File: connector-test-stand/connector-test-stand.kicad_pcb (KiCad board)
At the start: 2 copper layers, 99.1 x 99.1 mm, 85 parts, among them J1 Conn_01x02, J10 Conn_01x04_MountingPin, J11 Conn_01x03_MountingPin, J12 DVI-I_Dual_Link, J2 Conn_01x02, J3 Conn_01x02, J4 Conn_01x05, J5 Conn_01x04_MountingPin, J6 Conn_01x02, J7 Conn_01x03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

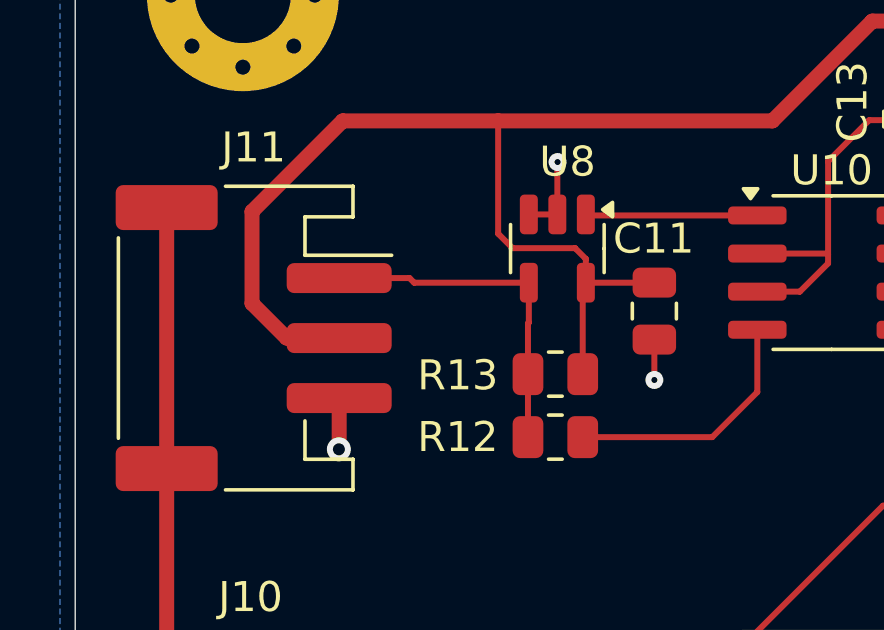
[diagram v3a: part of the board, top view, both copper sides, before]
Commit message: Add values for SMAART wire conevrter and safety rezistor
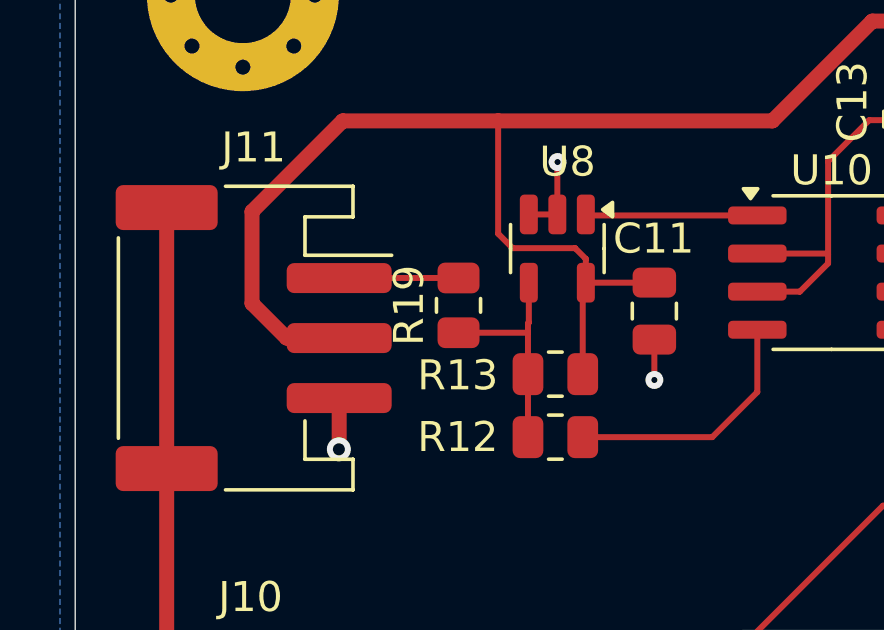
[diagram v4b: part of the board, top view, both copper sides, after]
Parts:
- added R19: 10R, Resistor_SMD:R_0805_2012Metric, F.Cu at (295.7, 121.1)
- R12: value R -> 100R
- R13: value R -> 4K1
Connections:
- R12 pad 2: Net-(J11-Pin_1) -> Net-(R12-Pad2)
- R13 pad 2: Net-(J11-Pin_1) -> Net-(R12-Pad2)
- U8 pad 4: Net-(J11-Pin_1) -> Net-(R12-Pad2)
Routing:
- net Net-(J11-Pin_1): track 11.5 -> 3.98 mm
- net Net-(R12-Pad2): track 0.00 -> 7.47 mm
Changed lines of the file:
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@@
 	(net 96 "TX")
 	(net 97 "Net-(U10-DE)")
+	(net 98 "Net-(R12-Pad2)")
 	(footprint "Potentiometer_THT:Potentiometer_Bourns_3266W_Vertical"
 		(layer "F.Cu")
@@
 			(layers "F.Cu" "F.Mask" "F.Paste")
 			(roundrect_rratio 0.25)
-			(net 51 "Net-(J11-Pin_1)")
+			(net 98 "Net-(R12-Pad2)")
 			(pintype "tri_state")
 		)
@@
 			)
 		)
-		(property "Value" "R"
+		(property "Value" "100R"
 			(at 0 1.65 0)
 			(layer "F.Fab")
@@
 			(layers "F.Cu" "F.Mask" "F.Paste")
 			(roundrect_rratio 0.243902)
-			(net 51 "Net-(J11-Pin_1)")
+			(net 98 "Net-(R12-Pad2)")
 			(pintype "passive")
 		)
@@
 			)
 		)
-		(property "Value" "R"
+		(property "Value" "4K1"
 			(at 0 1.65 0)
 			(layer "F.Fab")
@@
 			(layers "F.Cu" "F.Mask" "F.Paste")
 			(roundrect_rratio 0.243902)
-			(net 51 "Net-(J11-Pin_1)")
+			(net 98 "Net-(R12-Pad2)")
 			(pintype "passive")
 		)
@@
 		)
 	)
+	(footprint "Resistor_SMD:R_0805_2012Metric"
+		(layer "F.Cu")
+		(at 295.7322 121.0837 90)
+		(descr "Resistor SMD 0805 (2012 Metric), square (rectangular) end terminal, IPC-7351 nominal, (Body size source: IPC-SM-782 page 72, https://www.pcb-3d.com/wordpress/wp-content/uploads/ipc-sm-782a_amendment_1_and_2.pdf), generated with kicad-footprint-generator")
+		(tags "resistor")
+		(property "Reference" "R19"
+			(at 0 -1.65 90)
+			(layer "F.SilkS")
+			(effects
+				(font
+					(size 1 1)
+					(thickness 0.15)
+				)
+			)
+		)
+		(property "Value" "10R"
+			(at 0 1.65 90)
+			(layer "F.Fab")
+			(effects
+				(font
+					(size 1 1)
+					(thickness 0.15)
+				)
+			)
+		)
+		(property "Datasheet" ""
+			(at 0 0 90)
+			(layer "F.Fab")
+			(hide yes)
+			(effects
+				(font
+					(size 1.27 1.27)
+					(thickness 0.15)
+				)
+			)
+		)
+		(property "Description" "Resistor"
+			(at 0 0 90)
+			(layer "F.Fab")
+			(hide yes)
+			(effects
+				(font
+					(size 1.27 1.27)
+					(thickness 0.15)
+				)
+			)
+		)
+		(property ki_fp_filters "R_*")
+		(sheetname "/")
+		(sheetfile "connector-test-stand.kicad_sch")
+		(attr smd)
+		(fp_line
+			(start -0.227064 -0.735)
+			(end 0.227064 -0.735)
+			(stroke
+				(width 0.12)
+				(type solid)
+			)
+			(layer "F.SilkS")
+		)
+		(fp_line
+			(start -0.227064 0.735)
+			(end 0.227064 0.735)
+			(stroke
+				(width 0.12)
+				(type solid)
+			)
+			(layer "F.SilkS")
+		)
+		(fp_line
+			(start 1.68 -0.95)
+			(end 1.68 0.95)
+			(stroke
+				(width 0.05)
+				(type solid)
+			)
+			(layer "F.CrtYd")
+		)
+		(fp_line
+			(start -1.68 -0.95)
+			(end 1.68 -0.95)
+			(stroke
+				(width 0.05)
+				(type solid)
+			)
+			(layer "F.CrtYd")
+		)
+		(fp_line
+			(start 1.68 0.95)
+			(end -1.68 0.95)
+			(stroke
+				(width 0.05)
+				(type solid)
+			)
+			(layer "F.CrtYd")
+		)
+		(fp_line
+			(start -1.68 0.95)
+			(end -1.68 -0.95)
+			(stroke
+				(width 0.05)
+				(type solid)
+			)
+			(layer "F.CrtYd")
+		)
+		(fp_line
+			(start 1 -0.625)
+			(end 1 0.625)
+			(stroke
+				(width 0.1)
+				(type solid)
+			)
+			(layer "F.Fab")
+		)
+		(fp_line
+			(start -1 -0.625)
+			(end 1 -0.625)
+			(stroke
+				(width 0.1)
+				(type solid)
+			)
+			(layer "F.Fab")
+		)
+		(fp_line
+			(start 1 0.625)
+			(end -1 0.625)
+			(stroke
+				(width 0.1)
+				(type solid)
+			)
+			(layer "F.Fab")
+		)
+		(fp_line
+			(start -1 0.625)
+			(end -1 -0.625)
+			(stroke
+				(width 0.1)
+				(type solid)
+			)
+			(layer "F.Fab")
+		)
+		(fp_text user "${REFERENCE}"
+			(at 0 0 90)
+			(layer "F.Fab")
+			(effects
+				(font
+					(size 0.5 0.5)
+					(thickness 0.08)
+				)
+			)
+		)
+		(pad "1" smd roundrect
+			(at -0.9125 0 90)
+			(size 1.025 1.4)
+			(layers "F.Cu" "F.Mask" "F.Paste")
+			(roundrect_rratio 0.243902)
+			(net 98 "Net-(R12-Pad2)")
+			(pintype "passive")
+		)
+		(pad "2" smd roundrect
+			(at 0.9125 0 90)
+			(size 1.025 1.4)
+			(layers "F.Cu" "F.Mask" "F.Paste")
+			(roundrect_rratio 0.243902)
+			(net 51 "Net-(J11-Pin_1)")
+			(pintype "passive")
+		)
+		(embedded_fonts no)
+		(model "${KICAD9_3DMODEL_DIR}/Resistor_SMD.3dshapes/R_0805_2012Metric.step"
+			(offset
+				(xyz 0 0 0)
+			)
+			(scale
+				(xyz 1 1 1)
+			)
+			(rotate
+				(xyz 0 0 0)
+			)
+		)
+	)
 	(footprint "Capacitor_SMD:C_0805_2012Metric"
 		(layer "F.Cu")
@@
 	)
 	(segment
-		(start 294.2544 120.3284)
-		(end 298.0759 120.3284)
+		(start 295.7322 120.1712)
+		(end 291.7568 120.1712)
 		(width 0.2)
 		(layer "F.Cu")
@@
 	)
 	(segment
-		(start 294.1 120.174)
-		(end 294.2544 120.3284)
-		(width 0.2)
-		(layer "F.Cu")
-		(net 51)
-	)
-	(segment
-		(start 298.0474 123.3764)
-		(end 298.0474 121.6876)
-		(width 0.2)
-		(layer "F.Cu")
-		(net 51)
-	)
-	(segment
-		(start 291.754 120.174)
-		(end 294.1 120.174)
-		(width 0.2)
-		(layer "F.Cu")
-		(net 51)
-	)
-	(segment
-		(start 298.0759 121.6591)
-		(end 298.0759 120.3284)
-		(width 0.2)
-		(layer "F.Cu")
-		(net 51)
-	)
-	(segment
-		(start 298.0474 121.6876)
-		(end 298.0759 121.6591)
-		(width 0.2)
-		(layer "F.Cu")
-		(net 51)
-	)
-	(segment
-		(start 298.0474 125.476)
-		(end 298.0474 123.3764)
+		(start 291.7568 120.1712)
+		(end 291.754 120.174)
 		(width 0.2)
 		(layer "F.Cu")
@@
 		(net 97)
 	)
+	(segment
+		(start 298.0474 123.3764)
+		(end 298.0474 121.9962)
+		(width 0.2)
+		(layer "F.Cu")
+		(net 98)
+	)
+	(segment
+		(start 298.0474 121.9962)
+		(end 298.0474 121.6876)
+		(width 0.2)
+		(layer "F.Cu")
+		(net 98)
+	)
+	(segment
+		(start 298.0759 121.6591)
+		(end 298.0759 120.3284)
+		(width 0.2)
+		(layer "F.Cu")
+		(net 98)
+	)
+	(segment
+		(start 295.7322 121.9962)
+		(end 298.0474 121.9962)
+		(width 0.2)
+		(layer "F.Cu")
+		(net 98)
+	)
+	(segment
+		(start 298.0474 121.6876)
+		(end 298.0759 121.6591)
+		(width 0.2)
+		(layer "F.Cu")
+		(net 98)
+	)
+	(segment
+		(start 298.0474 125.476)
+		(end 298.0474 123.3764)
+		(width 0.2)
+		(layer "F.Cu")
+		(net 98)
+	)
 	(zone

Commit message: Rework connector test stand board
* Add values for elements
* Rework power supply
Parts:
- removed R7, R8: R, Resistor_SMD:R_0805_2012Metric
- removed RV2: R_Potentiometer, Potentiometer_THT:Potentiometer_Bourns_3266W_Vertical
- removed U3: REF5050AD, Package_SO:SOIC-8_3.9x4.9mm_P1.27mm
- added R20: 10R thick film, Resistor_SMD:R_0805_2012Metric, F.Cu at (126.4, 57.4)
- added R21: 10R thick film, Resistor_SMD:R_0805_2012Metric, F.Cu at (126.4, 60.8)
- added U12: CDSOT236-0504C, Package_TO_SOT_SMD:SOT-23-6, F.Cu at (130.7, 59.0)
- added U13: MCP1501-40xSN, Package_SO:SOIC-8_3.9x4.9mm_P1.27mm, F.Cu at (159.2, 73.5)
- C12, C13, C14, C15, C2, C5, C8: value C -> 100nF
- C7: value C -> 1000uF 16V; footprint Capacitor_SMD:C_0805_2012Metric -> Capacitor_SMD:CP_Elec_10x10
- R10, R11: value R -> 10K 1%
- R14, R15: value R -> 10K
- R17, R18: value R -> 330R
- RV1, RV4: value R_Potentiometer -> 1K
- RV3: value R_Potentiometer -> 12K
- moved C7 263.3 mm to (110.0, 49.4), turned to 180 degrees
- moved C2 212.5 mm to (159.2, 69.5), turned to 0 degrees
- moved R11 208.1 mm to (158.1, 80.6), turned to -90 degrees
- moved RV4 205.0 mm to (166.7, 79.7), turned to 0 degrees
- moved C1 202.2 mm to (104.2, 133.9)
- moved C12 202.2 mm to (136.7, 68.9)
- moved C3 202.2 mm to (136.7, 71.4)
- moved F1 202.2 mm to (109.2, 124.7)
- moved F3 202.2 mm to (165.1, 108.3)
- moved F6 202.2 mm to (145.1, 108.3)
- moved F8 202.2 mm to (131.8, 108.3)
- moved FB5 202.2 mm to (153.9, 59.1)
- moved FB6 202.2 mm to (150.8, 59.1)
- moved J1 202.2 mm to (104.2, 121.2)
- moved J12 202.2 mm to (162.3, 52.3)
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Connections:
- C11 pad 1: +3.3V -> +5V
- C12 pad 1: +12V -> +5V
- C13 pad 1: +3.3V -> +5V
- C14 pad 1: +3.3V -> +5V
- C15 pad 1: +3.3V -> +5V
- C2 pad 1: Net-(J4-Pin_1) -> +5V
- C3 pad 1: +3.3V -> +5V
- C4 pad 1: +3.3V -> +5V
- C5 pad 1: +3.3V -> +5V
- C6 pad 1: +3.3V -> +5V
- C7 pad 1: +12V -> +5V
- J10 pad 2: unconnected-(J10-Pin_2-Pad2) -> +5V
- J11 pad 2: +3.3V -> +5V
- J12 pad 14: +3.3V -> +5V
- J12 pad 15: +12V -> +5V
- J12 pad 18: +3.3V -> +5V
- J12 pad C2: +3.3V -> +5V
- J12 pad C4: +12V -> +5V
- J5 pad 2: +3.3V -> +5V
- J9 pad 2: unconnected-(J9-Pin_2-Pad2) -> +5V
- R1 pad 1: +3.3V -> +5V
- R13 pad 1: +3.3V -> +5V
- R14 pad 1: +3.3V -> +5V
- R15 pad 1: +3.3V -> +5V
- R16 pad 1: RS485 bus A -> Net-(U10-B)
- R16 pad 2: RS485 bus B -> Net-(U10-A)
- R17 pad 1: +12V -> +5V
- R18 pad 1: +12V -> +5V
- R3 pad 1: +3.3V -> +5V
- R5 pad 1: +3.3V -> +5V
- U1 pad 1: +3.3V -> +5V
- U10 pad 6: RS485 bus B -> Net-(U10-A)
- U10 pad 7: RS485 bus A -> Net-(U10-B)
- U10 pad 8: +3.3V -> +5V
- U11 pad 5: +3.3V -> +5V
- U2 pad 7: +3.3V -> +5V
- U4 pad 20: +3.3V -> +5V
- U5 pad 7: +3.3V -> +5V
- U6 pad 5: +3.3V -> +5V
- U8 pad 5: +3.3V -> +5V
- U9 pad 8: +12V -> +5V
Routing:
- net +5V: track 0.00 -> 559.0 mm, vias 0 -> 8
- net +3.3V: track 352.1 -> 0.00 mm, vias 8 -> 0
- net +12V: track 108.8 -> 0.00 mm, vias 5 -> 0
- net TEST_STAND_BAT_V: track 150.2 -> 130.8 mm
- net STRAIN_GAUGE_RETURN: track 35.9 -> 50.2 mm, vias 2 -> 0
- net Net-(U2-Ref): track 20.6 -> 8.74 mm
- net RS485 bus A: track 40.1 -> 31.4 mm
- net RS485 bus B: track 37.3 -> 28.7 mm
- net Net-(U10-A): track 0.00 -> 8.13 mm
- net Net-(U10-B): track 0.00 -> 7.47 mm
- net GND: track 114.6 -> 121.4 mm, vias 42 -> 46
- net Net-(R8-Pad1): track 4.78 -> 0.00 mm
- net Net-(U3-Trim/NR): track 3.30 -> 0.00 mm
- net Net-(R7-Pad1): track 2.24 -> 0.00 mm
- net Net-(U5-+): track 8.85 -> 10.3 mm
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
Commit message: Rework connector test stand
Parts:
- C1, C3, C4, C6, C9: value C -> 100nF
- C10: value C_Polarized -> 1000uF 16V
- J11: value Conn_01x03_MountingPin -> DE9_Socket_MountingHoles; footprint Connector_JST:JST_PH_S3B-PH-SM4-TB_1x03-1MP_P2.00mm_Horizontal -> Connector_Dsub:DSUB-9_Socket_Horizontal_P2.77x2.84mm_EdgePinOffset9.90mm_Housed_MountingHolesOffset11.32mm
- J8: footprint TerminalBlock_Altech:Altech_AK100_1x10_P5.00mm -> TerminalBlock_4Ucon:TerminalBlock_4Ucon_1x10_P3.50mm_Horizontal
- R9: value R -> 10K
- moved J9 54.7 mm to (128.5, 137.2), turned to 0 degrees
- moved J10 16.6 mm to (96.5, 93.3)
- moved J8 16.5 mm to (142.9, 138.2)
- moved J11 15.7 mm to (103.5, 74.4)
- moved C7 5.10 mm to (115.0, 50.3)
- moved C11 4.73 mm to (114.4, 60.4)
- moved R12 4.73 mm to (111.1, 64.6)
- moved R19 4.73 mm to (107.9, 60.2)
- moved U10 4.73 mm to (120.3, 59.1)
- moved U11 4.73 mm to (128.8, 54.0)
- moved U12 4.73 mm to (135.4, 59.9)
- moved R13 4.73 mm to (111.1, 62.5)
- moved C13 4.73 mm to (122.8, 54.0)
- moved C15 4.73 mm to (125.5, 54.0)
- moved R16 4.73 mm to (126.6, 59.1)
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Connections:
- J11 pad 1: Net-(J11-Pin_1) -> +5V
- J11 pad 2: +5V -> Net-(J11-Pad2)
- J11 pad 3: GND -> Net-(J11-Pad2)
- R19 pad 2: Net-(J11-Pin_1) -> Net-(J11-Pad2)
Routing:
- net SCL: track 92.7 -> 126.3 mm, vias 2 -> 3
- net SDA: track 93.5 -> 124.5 mm, vias 6 -> 5
- net GND: track 121.4 -> 96.7 mm, vias 46 -> 45
- net +5V: track 559.0 -> 581.1 mm, vias 8 -> 9
- net Net-(J11-Pad2): track 0.00 -> 14.2 mm
- net Net-(J8-Pin_2): track 16.6 -> 30.5 mm
- net Net-(J8-Pin_3): track 16.0 -> 27.5 mm
- net Net-(J8-Pin_4): track 15.3 -> 23.8 mm
- net RS485 transmit enable: track 26.3 -> 19.8 mm
- net Net-(J8-Pin_5): track 14.6 -> 20.7 mm
- net RS485 bus B: track 28.7 -> 23.6 mm
- net RS485 bus A: track 31.4 -> 26.4 mm
- net Net-(J11-Pin_1): track 3.98 -> 0.00 mm
- net Net-(J8-Pin_6): track 14.1 -> 17.9 mm
- net Net-(J8-Pin_7): track 14.8 -> 16.6 mm
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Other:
- board text added: "Battery"
- board text added: "Big Fucking Connector"
- board text added: "Extra I2C"
- board text added: "High-power IO"
- board text added: "Pressure 1"
- board text added: "Pressure 2"
- board text added: "SMAAART WIRE"
- board text added: "Servo"
- board text added: "Starter I2C"
- board text added: "Starter Power"
- board text added: "Starter Sense"
- board text added: "Tensometr"
